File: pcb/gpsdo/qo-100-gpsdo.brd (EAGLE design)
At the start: 100 x 69.5 mm, 266 parts, among them CON1 3P-SH-SIDE, CON2 4P-SH-TOP, CON3 3P-SH-TOP, CON4 2EDG-2P-5MM, J1 DCJACK, U1 EFM32GG11B120F2048GM64, U10 74LVC1G17, U11 74LVC1G17, U12 74LVC1G17, U13 74LVC1G17, U14 ADM7171ACPZ-1.8, U15 ADM7171ACPZ-5.0, U16 MIC23155, U17 LT8636, U18 ADM7171ACPZ-3.3, U19 74LVC1G17, U2 MAX-M8Q, U20 74LVC1G17, U3 MCP1501-40, U4 AD5541ACPZ, U5 MCP6V31, U6 OSC5A2B02, U7 DSB321SDA, U8 AD9544, U9 74LVC1G17

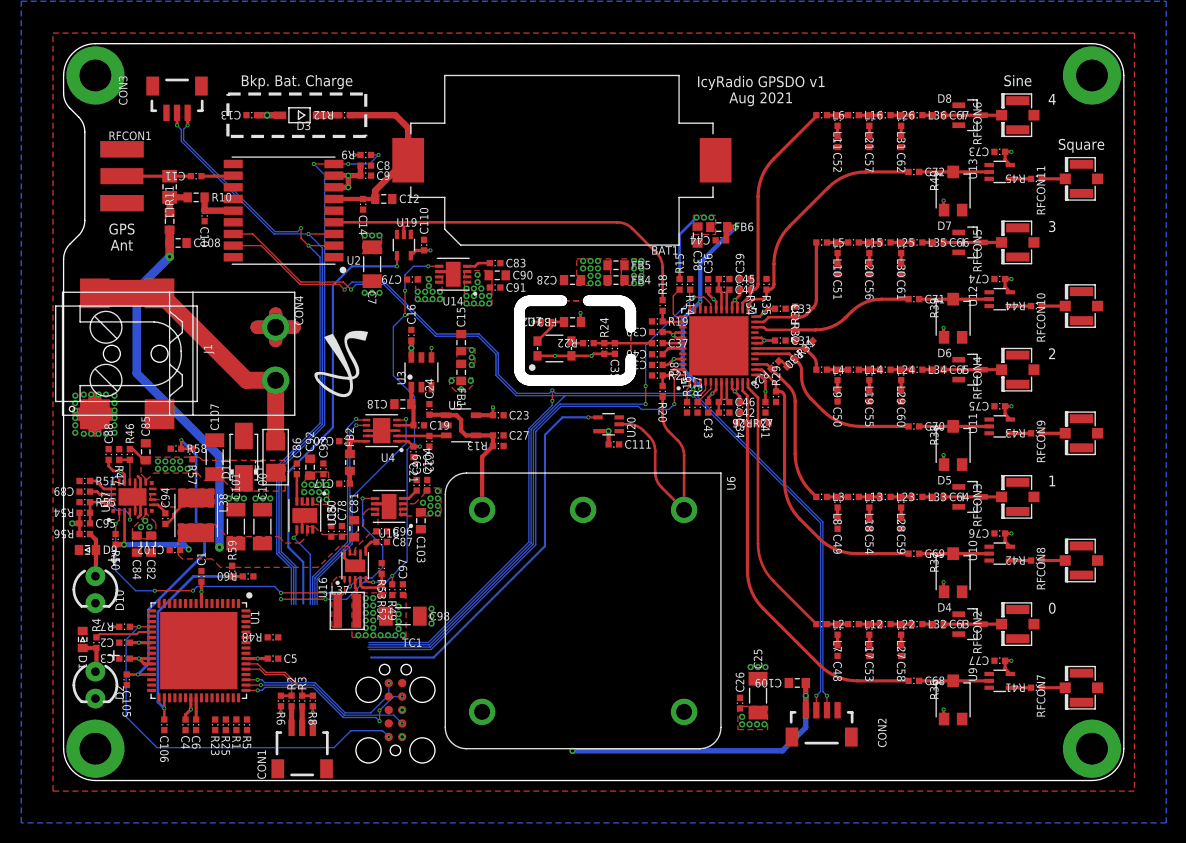
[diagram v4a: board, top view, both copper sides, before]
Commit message: Generate production files for GPSDO
Signed-off-by: João Silva <jgc3silva@gmail.com>
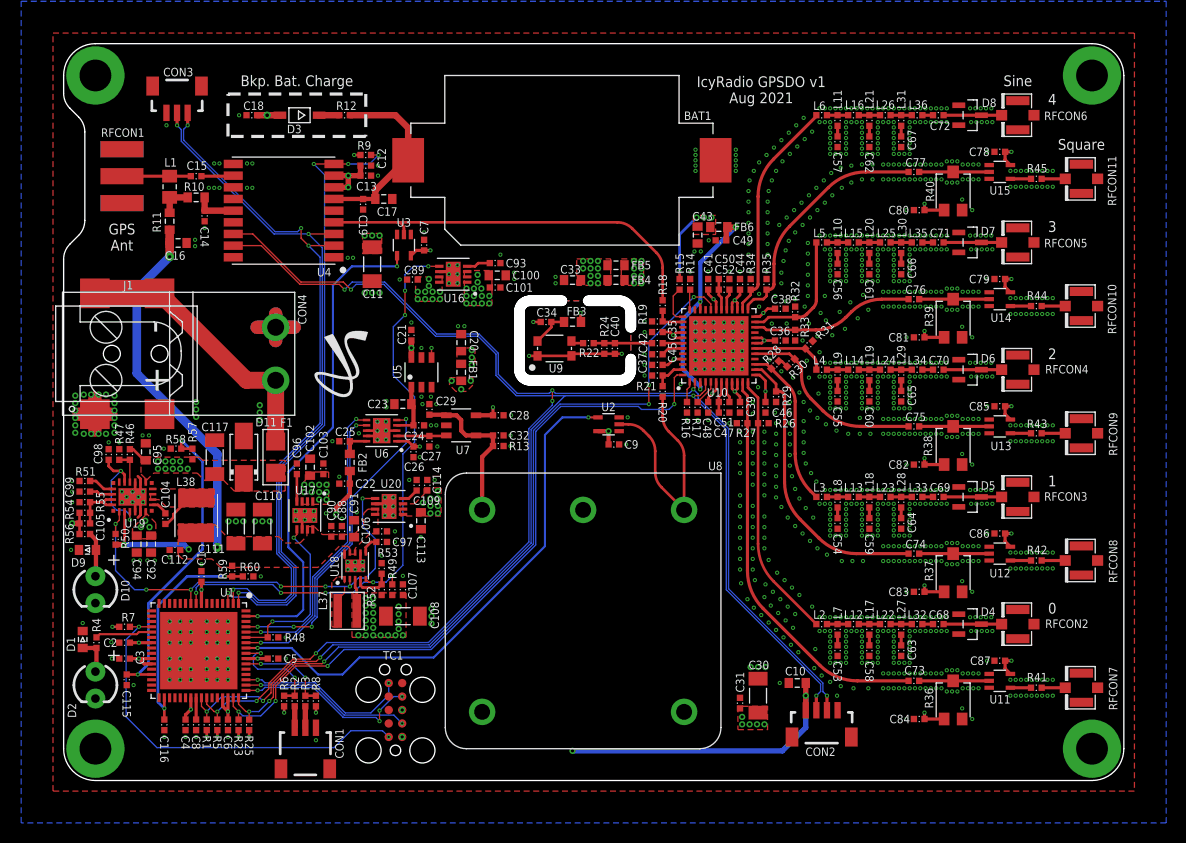
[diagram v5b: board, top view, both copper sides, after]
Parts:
- added C112, C114: 100nF, Capacitor:CAP0402
- added C113: 10uF, Capacitor:CAP0603
- added C115, C116: 470pF, Capacitor:CAP0402
- added C117: 10uF, Capacitor:CAP1206
- C10, C102, C20: value 100nF -> 10uF; device Capacitor:CAP0402 -> Capacitor:CAP0603
- C100: value 100uF -> 10uF; device Capacitor:CAP1206 -> Capacitor:CAP0603
- C101, C25, C7: value 100uF -> 100nF; device Capacitor:CAP1206 -> Capacitor:CAP0402
- C103, C12, C18, C90: value 10uF -> 100nF; device Capacitor:CAP0603 -> Capacitor:CAP0402
- C105: value 470pF -> 10pF
- C106: value 470pF -> 100nF
- C107: value 10uF -> 100nF; device Capacitor:CAP1206 -> Capacitor:CAP0402
- C108: value 10uF -> 100uF; device Capacitor:CAP0603 -> Capacitor:CAP1206
- C109: value 10uF -> 10nF; device Capacitor:CAP0603 -> Capacitor:CAP0402
- C11: value 47pF -> 100uF; device Capacitor:CAP0402 -> Capacitor:CAP1206
- C110, C111: value 100nF -> 100uF; device Capacitor:CAP0402 -> Capacitor:CAP1206
- C15: value 10uF -> 47pF; device Capacitor:CAP0603 -> Capacitor:CAP0402
- C16, C17, C23, C33, C43: value 1uF -> 10uF; device Capacitor:CAP0402 -> Capacitor:CAP0603
- C22, C26, C37, C78, C79, C8: value 100nF -> 1uF
- C28, C38: value 10uF -> 1uF; device Capacitor:CAP0603 -> Capacitor:CAP0402
- C29, C31, C32, C6, C73, C74, C75, C76, C77, C88: value 1uF -> 100nF
- C30: value 1uF -> 100uF; device Capacitor:CAP0402 -> Capacitor:CAP1206
- C35: value 10pF -> 1uF
- C40: value 100nF -> 10pF
- C42, C45: value 220nF -> 100nF
- C46: value 3.9nF -> 1uF
- C47: value 3.9nF -> 220nF
- C48, C49: value 270pF -> 1uF
- C50: value 270pF -> 220nF
- C51, C52: value 270pF -> 3.9nF
- C53, C54: value 220pF -> 270pF
- C55, C56: value 220pF -> 100pF
- C57, C60, C61: value 220pF -> 68pF
- C58, C59: value 220pF -> 180pF
- C62: value 220pF -> 47pF
- C63, C64: value 100nF -> 180pF
- C65, C66: value 100nF -> 68pF
- C67: value 100nF -> 47pF
- C81, C82: value 4.7uF -> 100nF; device Capacitor:CAP0603 -> Capacitor:CAP0402
- C83, C89: value 10nF -> 100nF
- C84: value 1uF -> 100nF; device Capacitor:CAP0603 -> Capacitor:CAP0402
- C85: device Capacitor:CAP0603 -> Capacitor:CAP0402
- C86: value 10nF -> 1uF
- C87: value 470pF -> 1uF
- C91: value 100nF -> 4.7uF; device Capacitor:CAP0402 -> Capacitor:CAP0603
- C92: value 10uF -> 4.7uF
- C93, C96: value 100nF -> 10nF
- C94: value 100nF -> 1uF; device Capacitor:CAP0402 -> Capacitor:CAP0603
- C95: value 10pF -> 1uF; device Capacitor:CAP0402 -> Capacitor:CAP0603
- C97: value 100nF -> 470pF
- C98: value 100uF -> 1uF; device Capacitor:CAP1206 -> Capacitor:CAP0402
- L10, L9: value 68nH -> 33nH
- L11: value 68nH -> 22nH
- L12, L13: value 1uH -> 820nH
- L14, L15: value 1uH -> 270nH
- L16: value 1uH -> 180nH
- L17, L18: value 330nH -> 470nH
- L19, L20: value 330nH -> 180nH
- L21: value 330nH -> 120nH
- L22, L23: value 820nH -> 680nH
- L24, L25: value 820nH -> 270nH
- L26: value 820nH -> 180nH
- L27, L28: value 220nH -> 330nH
- L29, L30: value 220nH -> 120nH
- L31: value 220nH -> 82nH
- L32, L33: value 470nH -> 390nH
- L34, L35: value 470nH -> 150nH
- L36: value 470nH -> 100nH
- L4, L5: value 560nH -> 220nH
- L6: value 560nH -> 150nH
- L7, L8: value 68nH -> 82nH
- R18: value 267 Ohms -> 280 Ohms
- R19: value 865 Ohms -> 330 Ohms
- R20: value 470 Ohms -> 510 Ohms
- R21: value 865 Ohms -> 270 Ohms
- R36, R37, R38, R39, R40: value 10K Ohms -> 100K Ohms
- U1: value EFM32GG11B120F2048GM64 -> EFM32GG11B420F2048GM64
- U10: value 74LVC1G17 -> AD9544; device Logic:SC70-5 -> Analog Devices:QFN48_2
- U14: value ADM7171ACPZ-1.8 -> 74LVC1G17; device Analog Devices:LFCSP8_3X3 -> Logic:SC70-5
- U15: value ADM7171ACPZ-5.0 -> 74LVC1G17; device Analog Devices:LFCSP8_3X3 -> Logic:SC70-5
- U16: value MIC23155 -> ADM7171ACPZ-1.8; device Microchip:DFN10 -> Analog Devices:LFCSP8_3X3
- U17: value LT8636 -> ADM7171ACPZ-5.0; device Analog Devices:QFN20_ASYM_3X4_CORNER -> Analog Devices:LFCSP8_3X3
- U18: value ADM7171ACPZ-3.3 -> MIC23155; device Analog Devices:LFCSP8_3X3 -> Microchip:DFN10
- U19: value 74LVC1G17 -> LT8636; device Logic:SC70-5 -> Analog Devices:QFN20_ASYM_3X4_CORNER
- U2: value MAX-M8Q -> 74LVC1G17; device U-Blox:MAX-M8 -> Logic:SC70-5
- U20: value 74LVC1G17 -> ADM7171ACPZ-3.3; device Logic:SC70-5 -> Analog Devices:LFCSP8_3X3
- U3: value MCP1501-40 -> 74LVC1G17; device Microchip:SOT23-6 -> Logic:SC70-5
- U4: value AD5541ACPZ -> MAX-M8Q; device Analog Devices:DFN10 -> U-Blox:MAX-M8
- U5: value MCP6V31 -> MCP1501-40; device Microchip:SOT23-5 -> Microchip:SOT23-6
- U6: value OSC5A2B02 -> AD5541ACPZ; device Crystal:OSC5A2B02 -> Analog Devices:DFN10
- U7: value DSB321SDA -> MCP6V31; device Crystal:TCXO-3225 -> Microchip:SOT23-5
- U8: value AD9544 -> OSC5A2B02; device Analog Devices:QFN48_2 -> Crystal:OSC5A2B02
- U9: value 74LVC1G17 -> DSB321SDA; device Logic:SC70-5 -> Crystal:TCXO-3225
- moved C85 80.7 mm to (88.3, 35.3), turned to 180 degrees
- moved C84 75.6 mm to (80.7, 5.80), turned to 180 degrees
- moved U15 73.1 mm to (88.3, 57.4)
- moved C82 72.8 mm to (80.7, 29.8), turned to 180 degrees
- moved C78 71.6 mm to (88.3, 59.3), turned to 180 degrees
- moved C10 71.2 mm to (69.2, 9.20), turned to 180 degrees
- moved C86 66.6 mm to (88.3, 23.3), turned to 180 degrees
- moved C80 63.2 mm to (80.7, 53.8), turned to 180 degrees
- moved C87 59.4 mm to (88.3, 11.3), turned to 180 degrees
- moved C81 56.3 mm to (80.7, 41.8), turned to 180 degrees
- moved C79 55.4 mm to (88.3, 47.3)
- moved C8 55.1 mm to (12.5, 5.25), turned to 270 degrees
- moved U9 52.4 mm to (46.3, 40.8), turned to 0 degrees
- moved U14 51.6 mm to (88.3, 45.4), turned to 270 degrees
- moved C83 50.6 mm to (80.7, 17.8), turned to 180 degrees
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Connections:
- net !CLK0: now also U10.12; no longer U8.12
- net !CLK1: now also U10.15; no longer U8.15
- net !CLK2: now also U10.18; no longer U8.18
- net !CLK3: now also U10.23; no longer U8.23
- net !CLK4: now also U10.26; no longer U8.26
- net !DAC_CS: now also U6.5; no longer U4.5
- net !GPS_RESET: now also U1.3, U4.9; no longer U2.9
- net !PLL_IRQ: now also U1.48, U10.32; no longer U1.46, U8.32
- net !PLL_RESET: now also U1.47, U10.48; no longer U1.45, U8.48
- net 1V8_PLL_CLEAN: now also C100.1, C101.1, C33.1, U16.1, U16.2, U16.3; no longer C28.1, C90.1, C91.1, U14.1, U14.2, U14.3
- net 1V8_PLL_CLEAN_FILT: now also C35.1, C37.1, C38.1, C44.1, C46.1, C48.1, U10.10, U10.13, U10.19, U10.20, U10.24, U10.27, U10.28, U10.31, U10.40, U10.41, U10.45, U10.6, U10.9; no longer C30.1, C31.1, C32.1, C33.1, C34.1, C43.1, U8.10, U8.13, U8.19, U8.20, U8.24, U8.27, U8.28, U8.31, U8.40, U8.41, U8.45, U8.6, U8.9
- net 3V3: now also C10.1, C107.1, C108.1, C11.1, C12.1, C18.1, C22.1, C43.1, C6.1, C89.1, U1.45, U1.46, U16.7, U16.8, U18.3, U2.5, U3.5, U4.7, U4.8; no longer C109.1, C110.1, C111.1, C17.1, C38.1, C79.1, C8.1, C97.1, C98.1, U14.7, U14.8, U16.3, U19.5, U2.7, U2.8, U20.5
- net 3V3_ANA_CLEAN: now also C113.1, C114.1, C78.1, C79.1, C80.1, C81.1, C82.1, C83.1, C84.1, C85.1, C86.1, C87.1, U14.5, U15.5, U20.1, U20.2, U20.3; no longer C103.1, C104.1, C73.1, C74.1, C75.1, C76.1, C77.1, U10.5, U18.1, U18.2, U18.3, U9.5
- net 3V3_FB: now also U18.4; no longer U16.4
- net 3V3_PGOOD: now also U1.9, U18.5; no longer U14.5
- net 3V3_PLL_FILT: now also C49.1, U10.3, U10.34; no longer C44.1, U8.3, U8.34
- net 3V3_SS: now also C97.1, U18.6; no longer C87.1, U16.6
- net 3V3_SW: now also U18.1; no longer U16.1
- net 5V0: now also C105.1, C106.1, C110.1, C111.1, C112.1, C16.1, C88.1, C90.1, C91.1, U17.7, U17.8, U18.9, U19.2, U20.7, U20.8; no longer C100.1, C101.1, C102.1, C108.1, C78.1, C80.1, C81.1, C95.1, C96.1, U15.7, U15.8, U16.8, U16.9, U17.2, U18.7
- net 5V0_ANA_OCXO_CLEAN: now also C102.1, C103.1, C20.1, C30.1, C31.1, U17.1, U17.2, U17.3, U8.5; no longer C15.1, C25.1, C26.1, C92.1, C93.1, U15.1, U15.2, U15.3, U6.5
- net 5V0_ANA_OCXO_CLEAN_FILT: now also C26.1, C28.1, U5.4, U5.6, U6.1, U7.5; no longer C16.1, C23.1, U3.4, U3.6, U4.1, U5.5
- net 5V0_BST: now also C104.2, U19.7; no longer C94.2, U17.7
- net 5V0_EN: now also U19.14; no longer U17.14
- net 5V0_FB: now also C105.2, U19.19, U19.20; no longer C95.2, U17.19, U17.20
- net 5V0_INTVCC: now also C98.1, U19.15, U19.3; no longer C88.1, U17.15, U17.3
- net 5V0_PGOOD: now also U1.10, U18.2, U19.1, U20.5; no longer U16.2, U17.1, U18.5
- net 5V0_RT: now also U19.17; no longer U17.17
- net 5V0_SS: now also C99.1, U19.18; no longer C89.1, U17.18
- net 5V0_SW: now also C104.1, U19.10, U19.8, U19.9; no longer C94.1, U17.10, U17.8, U17.9
- net 5V0_VSENSE: now also C116.1; no longer C106.1
- net CLK0: now also C73.1, U10.11; no longer C68.1, U8.11
- net CLK1: now also C74.1, U10.14; no longer C69.1, U8.14
- net CLK2: now also C75.1, U10.17; no longer C70.1, U8.17
- net CLK3: now also C76.1, U10.22; no longer C71.1, U8.22
- net CLK4: now also C77.1, U10.25; no longer C72.1, U8.25
- net DAC_DIN: now also U6.7; no longer U4.7
- net DAC_SCLK: now also U6.6; no longer U4.6
- net GND: now also C11.2, C112.2, C113.2, C114.2, C115.2, C116.2, C117.2, C37.2, C46.2, C47.2, C63.2, C64.2, C65.2, C66.2, C67.2, C94.2, C95.2, U10.49, U14.3, U15.3, U16.6, U16.9, U17.6, U17.9, U18.10, U18.11, U18.7, U19.12, U19.13, U19.21, U19.4, U19.5, U19.M1, U19.M2, U19.M3, U19.M4, U2.3, U20.6, U20.9, U4.1, U4.10, U4.12, U5.3, U5.5, U6.11, U6.3, U6.8, U6.9, U8.2, U9.1, U9.2; no longer C104.2, C105.2, C15.2, C42.2, C51.2, C52.2, C73.2, C74.2, C75.2, C76.2, C77.2, U10.3, U14.6, U14.9, U15.6, U15.9, U16.10, U16.11, U16.7, U17.12, U17.13, U17.21, U17.4, U17.5, U17.M1, U17.M2, U17.M3, U17.M4, U18.6, U18.9, U19.3, U2.1, U2.10, U2.12, U20.3, U3.2, U3.5, U4.11, U4.3, U4.8, U4.9, U6.2, U7.1, U8.49, U9.3
- net GPS_BIAS_INT: now also C14.1, U4.14; no longer C10.1, U2.14
- net GPS_RXD: now also U1.1, U4.3; no longer U2.3
- net GPS_TIMEPULSE: now also U3.2, U4.4; no longer U19.2, U2.4
- net GPS_TIMEPULSE_BUF: now also U1.63, U3.4; no longer U19.4
- net GPS_TXD/TXREADY: now also U1.2, U4.2; no longer U2.2
- net GPS_VBKP: now also C17.1, C19.1, U4.6; no longer C12.1, C14.1, U2.6
- net I2C0_SCL: now also U1.42, U10.2, U4.17; no longer U1.48, U2.17, U8.2
- net I2C0_SDA: now also U1.41, U10.4, U4.16; no longer U1.47, U2.16, U8.4
- net I2C2_SDA: now also U1.56; no longer U1.53
- net MCU_VCORE: now also C8.1; no longer C6.1
- net N$1: now also C53.1; no longer C48.1
- net N$10: now also C69.2; no longer C64.2
- net N$103: now also C34.1, U9.4; no longer C29.1, U7.4
- net N$105: now also C93.1, U16.4; no longer C83.1, U14.4
- net N$12: now also C15.1, U4.11; no longer C11.1, U2.11
- net N$13: now also C15.2; no longer C11.2
- net N$16: now also C77.2, U15.2; no longer C72.2, U13.2
- net N$17: now also C40.1, C42.1; no longer C35.1, C37.1
- net N$18: now also U9.3; no longer U7.3
- net N$2: now also C58.1; no longer C53.1
- net N$20: now also C50.1, C52.1, U10.30; no longer C45.1, C47.1, U8.30
- net N$21: now also C47.1, C51.1, U10.7; no longer C42.1, C46.1, U8.7
- net N$22: now also C52.2, U10.29; no longer C47.2, U8.29
- net N$23: now also C51.2, U10.8; no longer C46.2, U8.8
- net N$24: now also U15.4; no longer U13.4
- net N$26: now also C109.1, U20.4; no longer C99.1, U18.4
- net N$27: now also C25.1, U6.10; no longer C20.1, U4.10
- net N$28: now also C96.1, U17.4; no longer C86.1, U15.4
- net N$29: now also U14.4; no longer U12.4
- net N$3: now also C63.1; no longer C58.1
- net N$30: now also C45.1, U10.43; no longer C40.1, U8.43
- net N$32: now also C76.2, U14.2; no longer C71.2, U12.2
- net N$34: now also C54.1; no longer C49.1
- net N$35: now also C59.1; no longer C54.1
- net N$36: now also C64.1; no longer C59.1
- net N$37: now also C23.1, C24.1, U5.1, U6.4; no longer C18.1, C19.1, U3.1, U4.4
- net N$38: now also C69.1; no longer C64.1
- net N$4: now also C68.1; no longer C63.1
- net N$41: now also C68.2; no longer C63.2
- net N$45: now also C70.2; no longer C65.2
- net N$47: now also C55.1; no longer C50.1
- net N$48: now also C60.1; no longer C55.1
- net N$49: now also C65.1; no longer C60.1
- net N$50: now also C70.1; no longer C65.1
- net N$53: now also C71.2; no longer C66.2
- net N$55: now also C56.1; no longer C51.1
- net N$56: now also C61.1; no longer C56.1
- net N$57: now also C66.1; no longer C61.1
- net N$58: now also C71.1; no longer C66.1
- net N$61: now also C72.2; no longer C67.2
- net N$63: now also C57.1; no longer C52.1
- net N$64: now also C62.1; no longer C57.1
- net N$65: now also C67.1; no longer C62.1
- net N$66: now also C72.1; no longer C67.1
- net N$68: now also U13.4; no longer U11.4
- net N$69: now also C75.2, U13.2; no longer C70.2, U11.2
- net N$7: now also C27.1, U6.2, U7.3; no longer C22.1, U4.2, U5.3
- net N$71: now also U12.4; no longer U10.4
- net N$72: now also C74.2, U12.2; no longer C69.2, U10.2
- net N$74: now also U11.4; no longer U9.4
- net N$75: now also C73.2, U11.2; no longer C68.2, U9.2
- net N$91: now also C42.2, U10.42; no longer C37.2, U8.42
- net OCXO_CLK: now also U2.2, U8.1; no longer U20.2, U6.1
- net OCXO_CLK_BUF: now also U1.57, U2.4; no longer U20.4
- net OCXO_EN: now also U17.5; no longer U15.5
- net OCXO_VCONT: now also C29.1, C32.1, U7.1, U7.4, U8.3; no longer C24.1, C27.1, U5.1, U5.4, U6.3
- net PLL_M3: now also U10.36; no longer U8.36
- net PLL_M4: now also U10.37; no longer U8.37
- net PLL_M5: now also U10.1; no longer U8.1
- net PLL_M6: now also U10.5; no longer U8.5
- net PLL_REFA: now also U10.47; no longer U8.47
- net PLL_REFB: now also U10.38; no longer U8.38
- net VIN: now also C117.1, C92.1, C94.1, C95.1, U19.11, U19.6; no longer C107.1, C82.1, C84.1, C85.1, U17.11, U17.6
- net VIN_VSENSE: now also C115.1; no longer C105.1
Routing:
- net I2C0_SDA: track 122.7 -> 143.7 mm, vias 3 -> 6
- net I2C0_SCL: track 121.8 -> 141.8 mm, vias 5 -> 8
- net !PLL_RESET: track 48.3 -> 66.4 mm, vias 1 -> 4
- net !PLL_IRQ: track 56.4 -> 73.6 mm, vias 3 -> 6
- net OCXO_CLK_BUF: track 36.9 -> 50.4 mm, vias 1 -> 2
- net 3V3: track 120.3 -> 133.0 mm, vias 55 -> 61
- net 3V3_PGOOD: track 47.2 -> 56.8 mm, vias 7 -> 8
- net DAC_DIN: track 19.5 -> 28.1 mm, vias 1 -> 2
- net !DAC_CS: track 21.9 -> 30.4 mm, vias 1 -> 4
- net OCXO_EN: track 7.86 -> 16.4 mm, vias 1 -> 2
- net 3V3_ANA_CLEAN: track 14.9 -> 23.0 mm
- net DAC_SCLK: track 20.2 -> 28.2 mm, vias 1 -> 2
- net !GPS_RESET: track 51.4 -> 58.8 mm, vias 3 -> 4
- net GPS_TXD/TXREADY: track 58.4 -> 65.0 mm, vias 3 -> 4
- net GPS_TIMEPULSE_BUF: track 40.1 -> 46.4 mm, vias 1 -> 2
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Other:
- board text added: "+"
- board text added: "-"

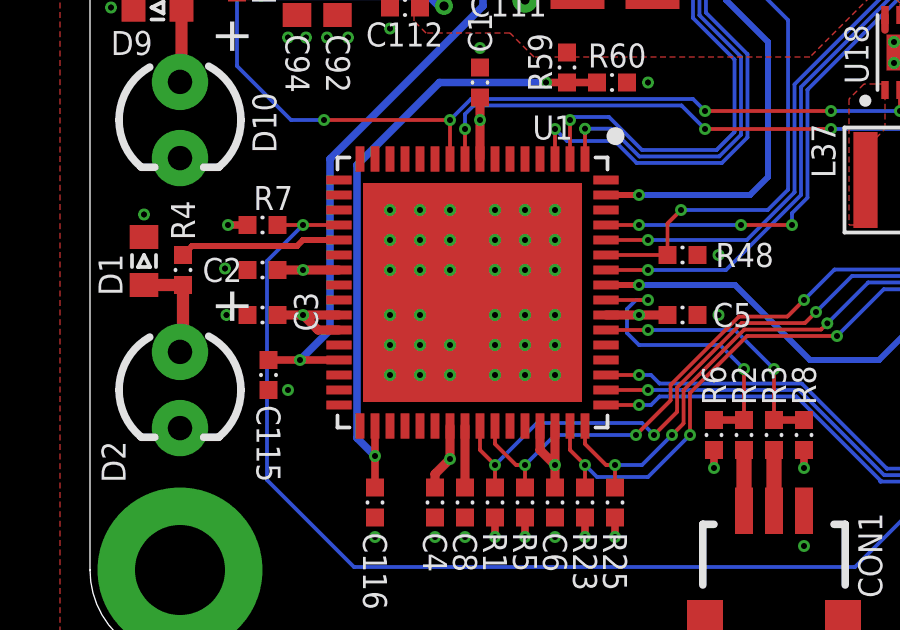
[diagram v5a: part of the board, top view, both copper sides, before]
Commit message: Add missing via under MCU in GPSDO Generate new gerbers
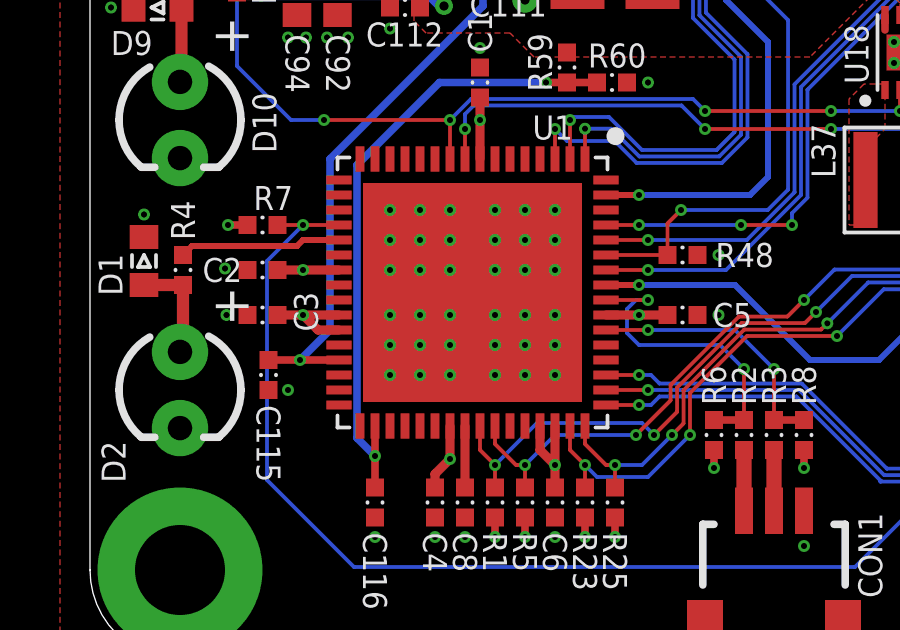
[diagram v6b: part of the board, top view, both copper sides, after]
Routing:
- net GND: vias 1262 -> 1263
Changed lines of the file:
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@@
 </attributes>
 <variantdefs>
-<variantdef name="jlcpcb_assembly"/>
 </variantdefs>
 <classes>
@@
 <via x="65.5" y="37.1" extent="1-16" drill="0.2"/>
 <via x="58.2" y="37.4" extent="1-16" drill="0.2"/>
+<via x="12" y="11.5" extent="1-16" drill="0.2"/>
 </signal>
 <signal name="3V3">

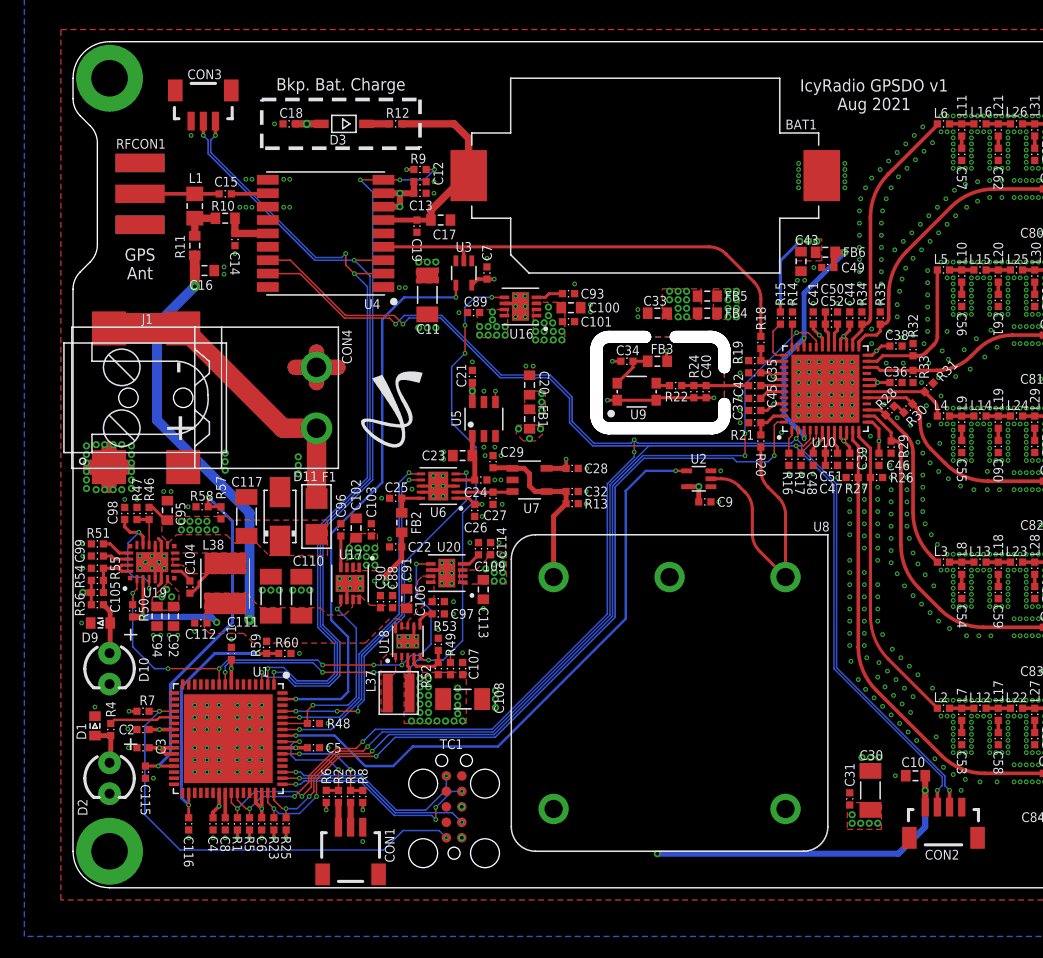
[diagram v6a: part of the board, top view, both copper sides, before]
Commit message: Rework GPSDO to fit a BGA MCU instead of a QFN since it is unobtanium
Signed-off-by: João Silva <jgc3silva@gmail.com>
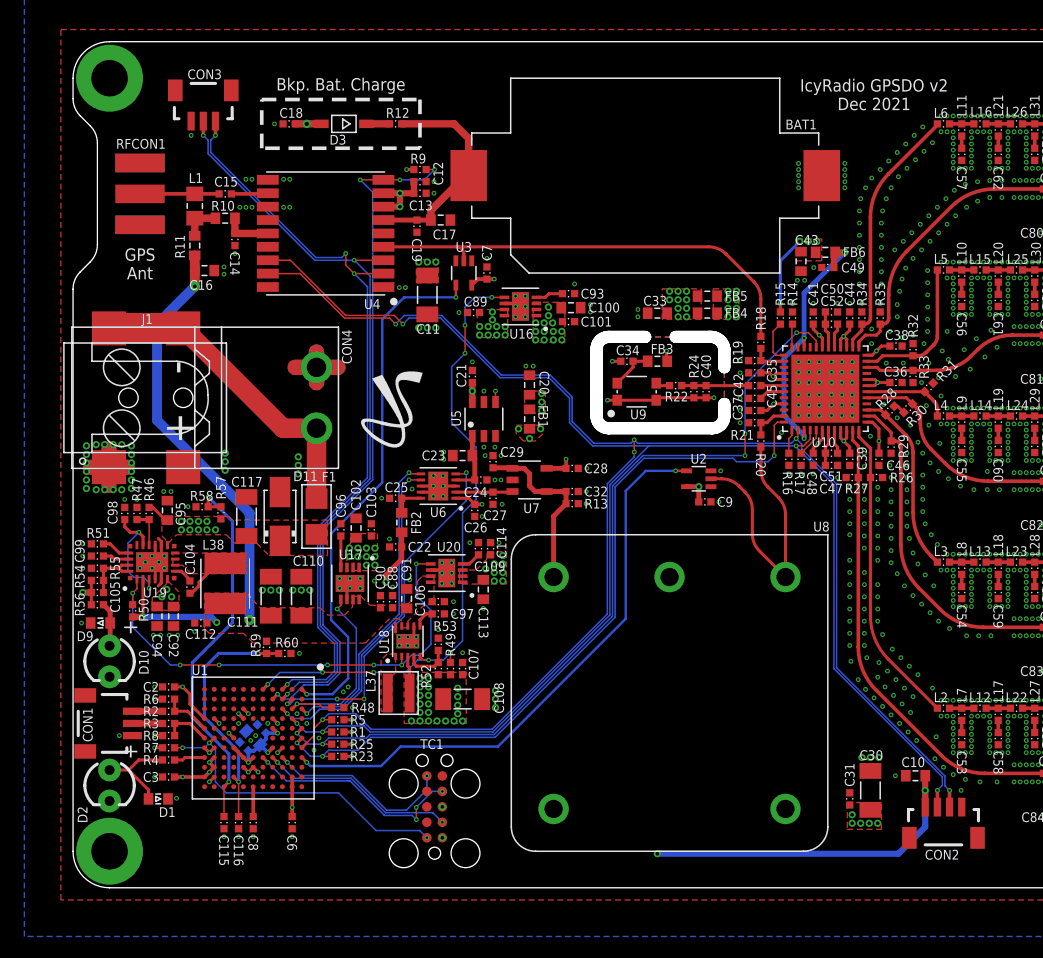
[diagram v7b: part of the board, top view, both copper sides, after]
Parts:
- C1: value 100nF -> 10uF; device Capacitor:CAP0402 -> Capacitor:CAP0603
- U1: value EFM32GG11B420F2048GM64 -> EFM32GG11B420F2048GL112; device EFM32:QFN64 -> EFM32:BGA112
- moved CON1 23.9 mm to (1.90, 13.5), turned to 270 degrees
- moved R8 16.7 mm to (7.85, 12.5), turned to 180 degrees
- moved R3 16.1 mm to (7.85, 13.5), turned to 0 degrees
- moved R2 15.6 mm to (7.85, 14.5), turned to 0 degrees
- moved R6 15.2 mm to (7.85, 15.5), turned to 180 degrees
- moved R5 11.2 mm to (21.8, 13.8), turned to 0 degrees
- moved R1 11.2 mm to (21.8, 12.8), turned to 0 degrees
- moved C4 8.77 mm to (15.5, 13.1), flipped to the bottom, turned to 45 degrees
- moved D1 7.94 mm to (7.00, 7.30), turned to 180 degrees
- moved R25 7.81 mm to (21.8, 11.8), turned to 0 degrees
- moved C115 7.67 mm to (12.4, 5.35)
- moved R23 7.64 mm to (21.8, 10.8), turned to 0 degrees
- moved C1 7.18 mm to (14.8, 12.3), flipped to the bottom, turned to 45 degrees
- moved C5 5.70 mm to (14.1, 11.6), flipped to the bottom, turned to 45 degrees
- moved R4 5.37 mm to (7.85, 10.5), turned to 0 degrees
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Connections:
- removed net I2C0_SCL: CON2.3, R5.1, U1.42, U10.2, U4.17
- removed net I2C0_SDA: CON2.2, R1.1, U1.41, U10.4, U4.16
- new net I2C1_SCL: R3.2, R8.1, U1.L6
- new net I2C1_SDA: R2.2, R6.1, U1.L5
- net !DAC_CS: now also U1.B2; no longer U1.61
- net !GPS_RESET: now also U1.D2; no longer U1.3
- net !MCU_RESET: now also U1.K6; no longer U1.20
- net !PLL_IRQ: now also U1.A5; no longer U1.48
- net !PLL_RESET: now also U1.A6; no longer U1.47
- net 3V3: now also U1.B10, U1.B11, U1.D5, U1.D7, U1.F8, U1.G4, U1.G8, U1.H7, U1.K8, U1.K9, U1.L10, U1.L4; no longer U1.23, U1.26, U1.27, U1.39, U1.45, U1.46, U1.55, U1.8
- net 3V3_PGOOD: now also U1.E1; no longer U1.9
- net 5V0_PGOOD: no longer U1.10
- net 5V0_VSENSE: now also U1.H10; no longer U1.34
- net DAC_DIN: now also U1.C3; no longer U1.58
- net DAC_SCLK: now also U1.A3; no longer U1.60
- net GND: now also U1.C7, U1.D4, U1.F9, U1.G3, U1.G9, U1.H6, U1.K10, U1.K4, U1.K7, U1.L7; no longer U1.65
- net GPS_RXD: now also U1.C2; no longer U1.1
- net GPS_TIMEPULSE_BUF: now also U1.A1; no longer U1.63
- net GPS_TXD/TXREADY: now also U1.C1; no longer U1.2
- net I2C2_SCL: now also CON2.3, R5.1, U1.A7, U10.2, U4.17; no longer R3.2, R8.1, U1.54
- net I2C2_SDA: now also CON2.2, R1.1, U1.B4, U10.4, U4.16; no longer R2.2, R6.1, U1.56
- net MCU_LED: now also U1.L8; no longer U1.21
- net MCU_SWCLK: now also U1.E8; no longer U1.49
- net MCU_SWDIO: now also U1.D8; no longer U1.50
- net MCU_SWO: now also U1.C8; no longer U1.51
- net MCU_VCORE: now also U1.F11; no longer U1.40
- net OCXO_CLK_BUF: now also U1.A8; no longer U1.57
- net OCXO_EN: now also U1.B3; no longer U1.59
- net VIN_VSENSE: now also U1.J11; no longer U1.29
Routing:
- net I2C0_SDA: track 143.7 -> 0.00 mm, vias 6 -> 0
- net I2C0_SCL: track 141.8 -> 0.00 mm, vias 8 -> 0
- net I2C2_SCL: track 8.84 -> 134.6 mm, vias 2 -> 6
- net I2C2_SDA: track 10.1 -> 135.2 mm, vias 2 -> 5
- net !MCU_RESET: track 37.9 -> 26.3 mm, vias 2 -> 3
- net 3V3: track 133.0 -> 140.3 mm, vias 61 -> 64
- net !PLL_RESET: track 66.4 -> 61.1 mm, vias 4 -> 3
- net GND: track 73.0 -> 78.2 mm, vias 1263 -> 1243
- net !PLL_IRQ: track 73.6 -> 68.9 mm, vias 6 -> 5
- net 3V3_PGOOD: track 56.8 -> 52.4 mm
- net N$144: track 3.57 -> 7.74 mm
- net I2C1_SDA: track 0.00 -> 4.03 mm
- net I2C1_SCL: track 0.00 -> 3.95 mm
- net MCU_LED: track 5.41 -> 2.53 mm
- net GPS_TXD/TXREADY: track 65.0 -> 62.1 mm
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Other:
- board text added: "IcyRadio GPSDO v2 Dec 2021"
- board text removed: "IcyRadio GPSDO v1 Aug 2021"
